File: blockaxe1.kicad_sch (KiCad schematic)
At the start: 16 parts, among them J5 54-00164

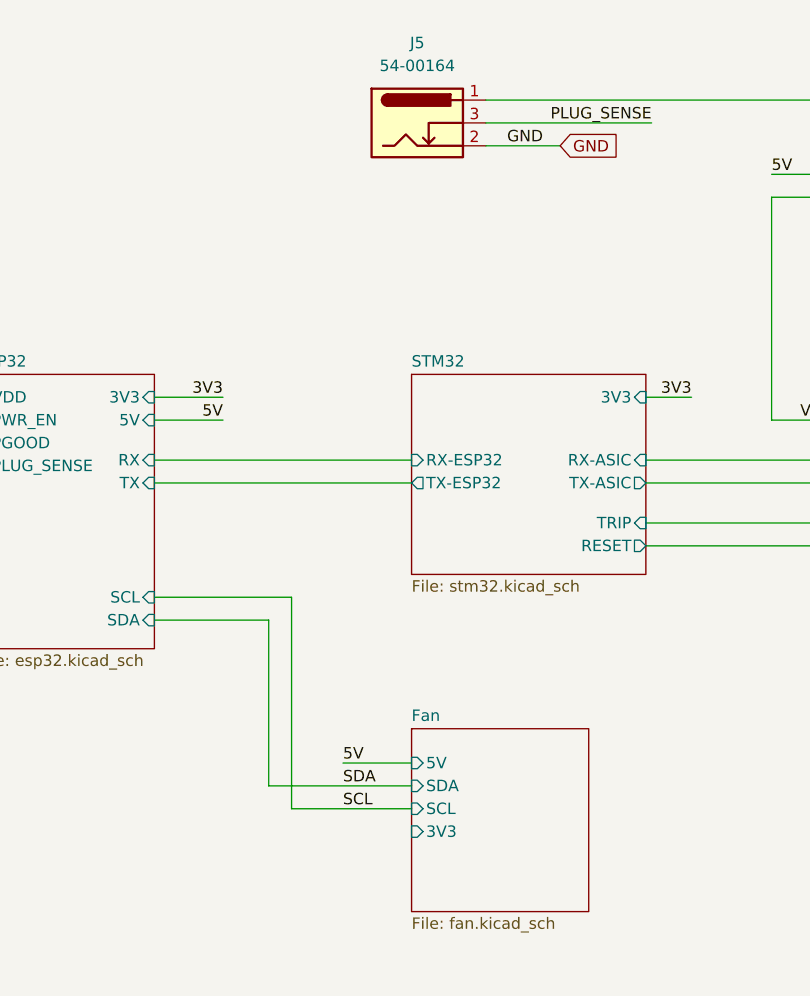
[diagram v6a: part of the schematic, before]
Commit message: finished routing. switched back to THT barrel
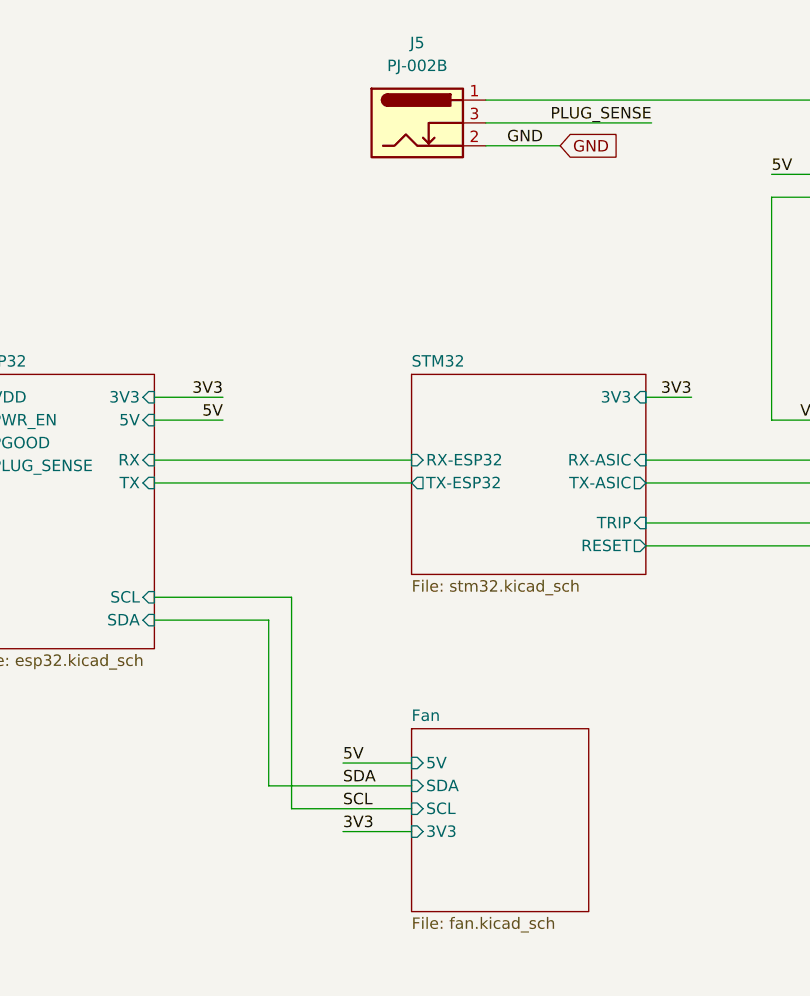
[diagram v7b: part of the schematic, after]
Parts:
- J5: value 54-00164 -> PJ-002B; footprint blockaxe:BarrelJack_Wuerth_694106106102_2.0x5.5mm -> blockaxe:CUI_PJ-002B; DK 839-54-00164CT-ND -> CP-002B-ND; PARTNO 54-00164 -> PJ-002B
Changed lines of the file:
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@@
     (stroke (width 0) (type default))
+  )
+  (wire (pts (xy 120.65 117.475) (xy 128.27 117.475))
+    (stroke (width 0) (type default))
+  )
+  (label "3V3" (at 120.65 117.475 0) (fields_autoplaced)
+    (effects (font (size 1.27 1.27)) (justify left bottom))
   )
   (label "3V3" (at 201.93 71.755 180) (fields_autoplaced)
@@
       (effects (font (size 1.27 1.27)))
     )
-    (property "Value" "54-00164" (at 128.905 32.385 0)
+    (property "Value" "PJ-002B" (at 128.905 32.385 0)
       (effects (font (size 1.27 1.27)))
     )
-    (property "Footprint" "blockaxe:BarrelJack_Wuerth_694106106102_2.0x5.5mm" (at 130.175 39.751 0)
+    (property "Footprint" "blockaxe:CUI_PJ-002B" (at 130.175 39.751 0)
       (effects (font (size 1.27 1.27)) hide)
     )
-    (property "Datasheet" "https://tensility.s3.amazonaws.com/uploads/pdffiles/54-00164.pdf?X-Amz-Expires=600&X-Amz-Date=20231120T033415Z&X-Amz-Algorithm=AWS4-HMAC-SHA256&X-Amz-Credential=AKIAIS2S4WRDQDSWDRZQ%2F20231120%2Fus-west-2%2Fs3%2Faws4_request&X-Amz-SignedHeaders=host&X-Amz-Signature=0ec7ce6b9e4957ccc83a05eb1138fede41cc8592648d2aac3c65914c1c151ca7" (at 130.175 39.751 0)
+    (property "Datasheet" "https://www.cuidevices.com/product/resource/pj-002b.pdf" (at 130.175 39.751 0)
       (effects (font (size 1.27 1.27)) hide)
     )
-    (property "DK" "839-54-00164CT-ND" (at 128.905 38.735 0)
+    (property "DK" "CP-002B-ND" (at 128.905 38.735 0)
       (effects (font (size 1.27 1.27)) hide)
     )
-    (property "PARTNO" "54-00164" (at 128.905 38.735 0)
+    (property "PARTNO" "PJ-002B" (at 128.905 38.735 0)
       (effects (font (size 1.27 1.27)) hide)
     )

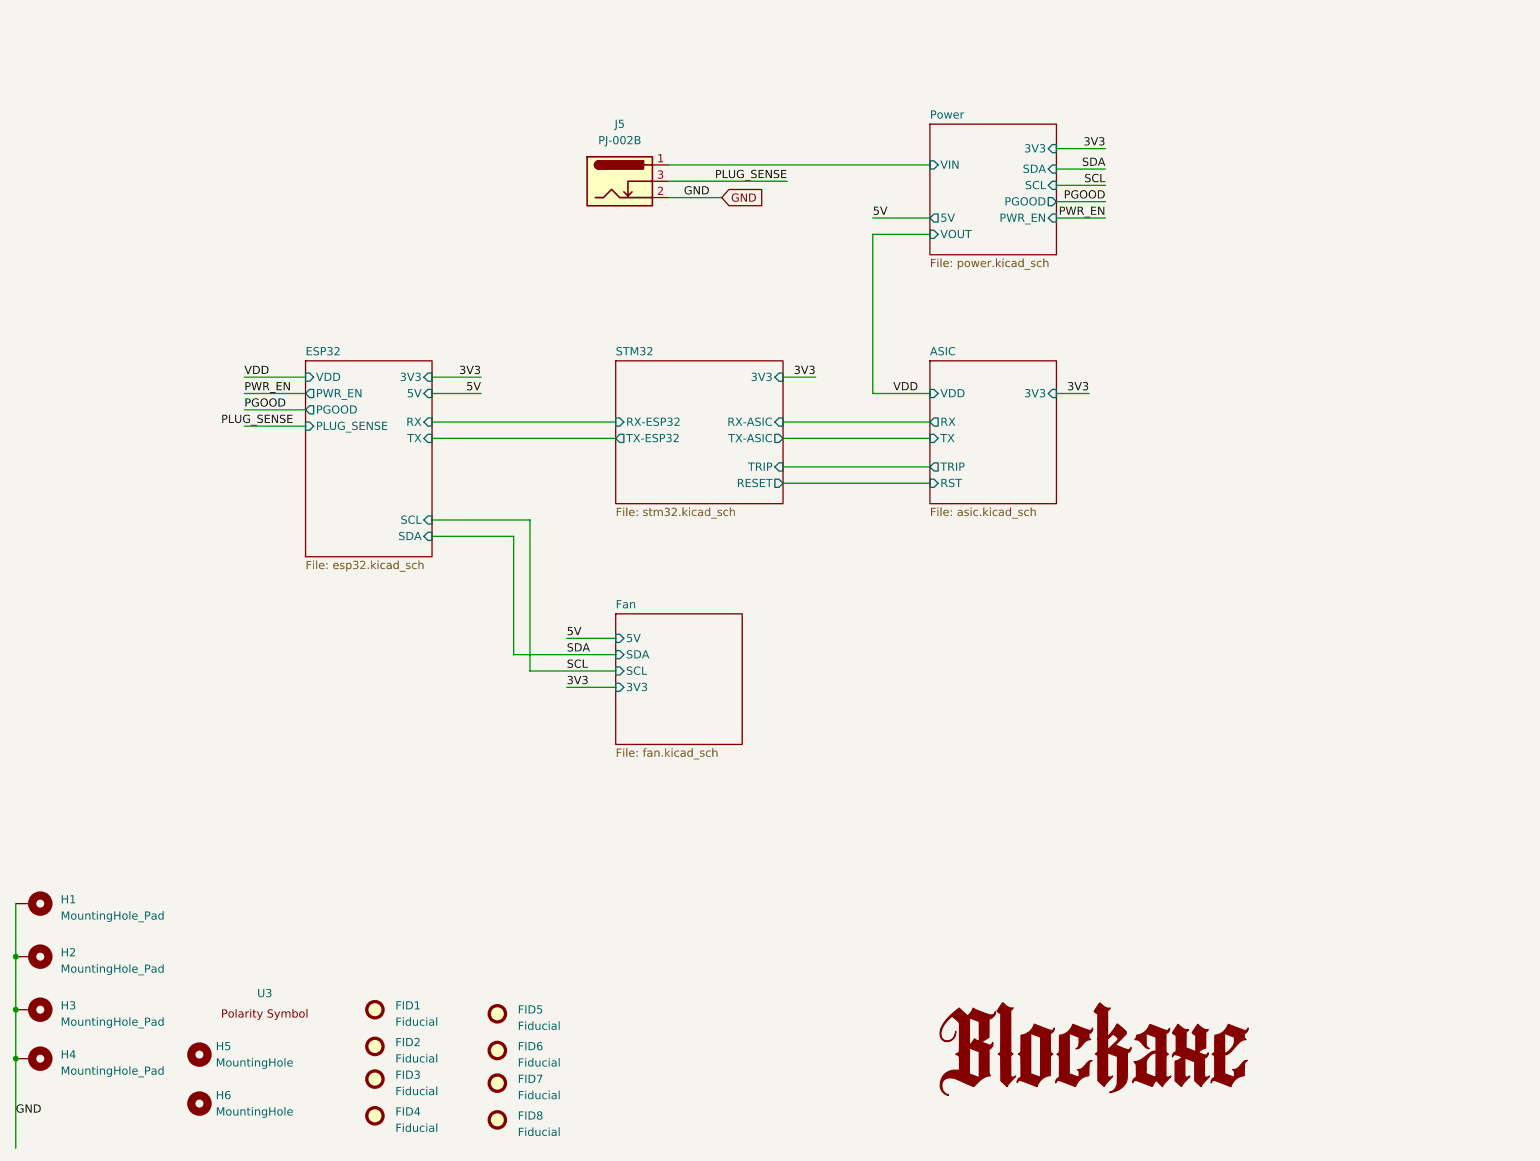
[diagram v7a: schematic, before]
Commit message: changed buttons for #5 flipped display for #2
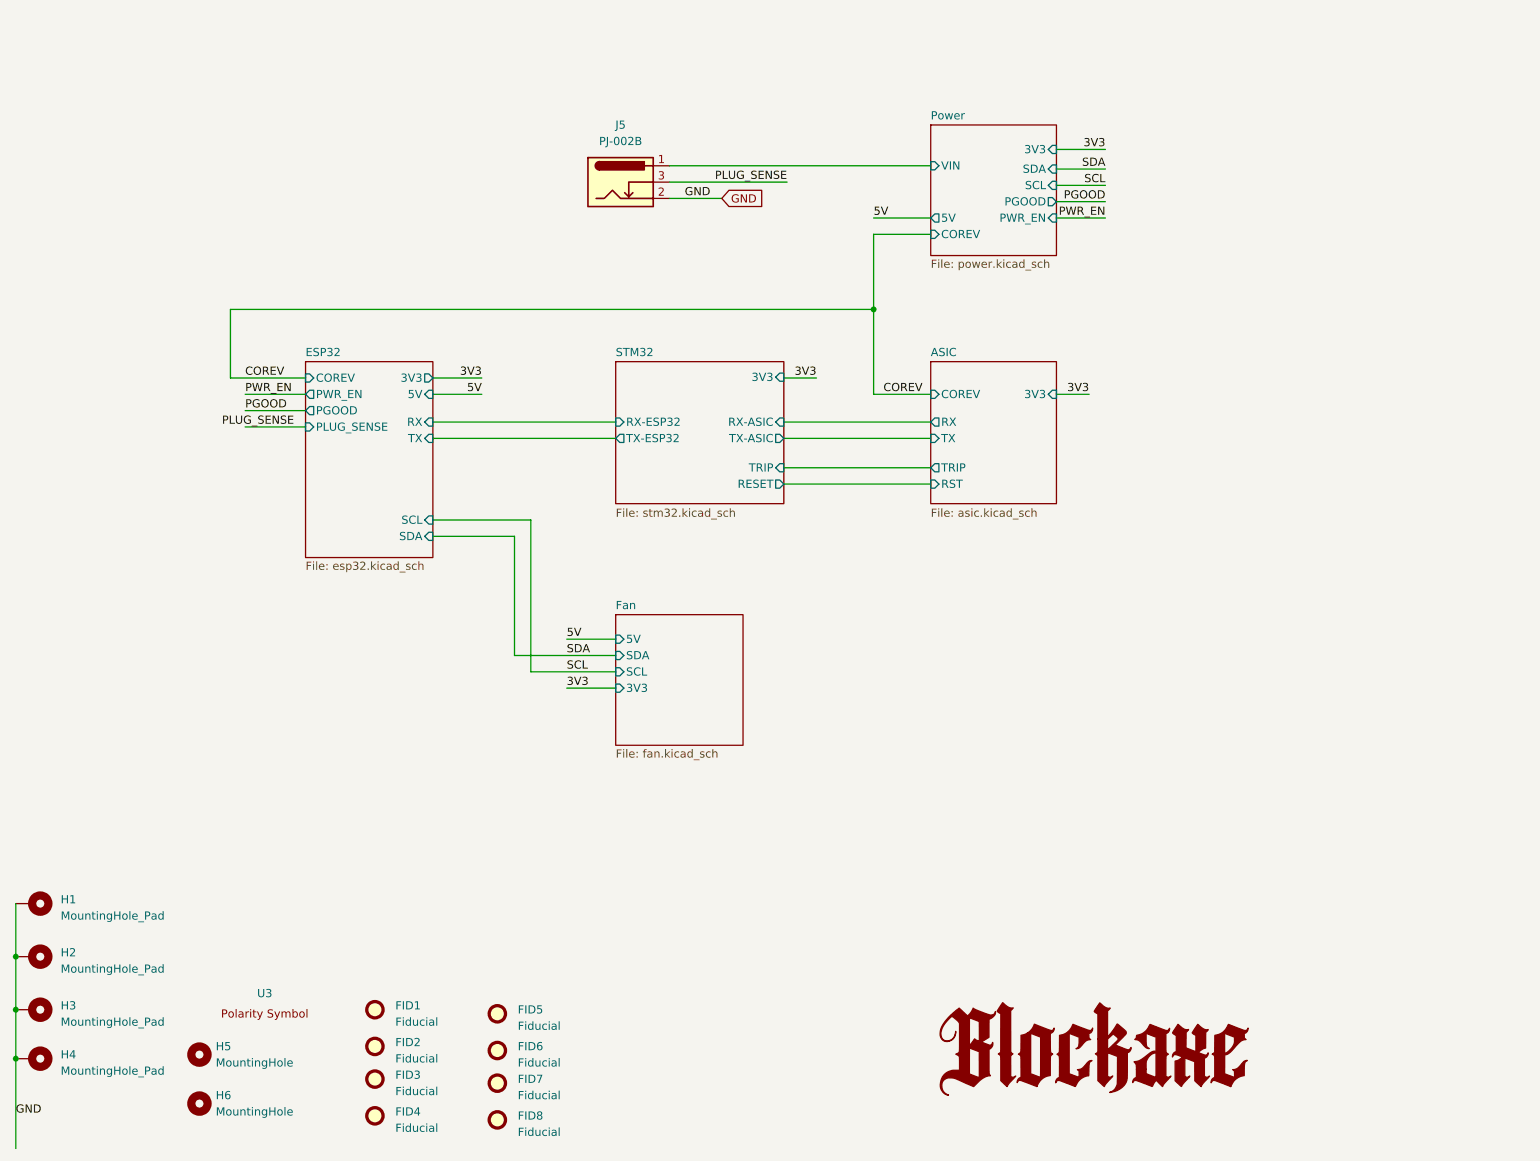
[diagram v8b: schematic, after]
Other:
- sheet ASIC ports: added COREV; removed VDD
- sheet ESP32 ports: added COREV; removed VDD
- sheet Power ports: added COREV; removed VOUT
